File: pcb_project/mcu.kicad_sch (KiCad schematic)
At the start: 29 parts, among them J3 Conn_ST_STDC14, SW2 SW_SPDT, SW3 SW_SPST, U2 STM32U595VJTx, Y1 48MHz

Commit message: Fix more footprints and add MicroSD reader 3D model
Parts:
- C76, C77: footprint (none) -> Capacitor_SMD:C_0603_1608Metric_Pad1.08x0.95mm_HandSolder
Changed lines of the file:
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@@
 			)
 		)
-		(property "Footprint" ""
+		(property "Footprint" "Capacitor_SMD:C_0603_1608Metric_Pad1.08x0.95mm_HandSolder"
 			(at 181.61 20.6248 0)
 			(effects
@@
 			)
 		)
-		(property "Footprint" ""
+		(property "Footprint" "Capacitor_SMD:C_0603_1608Metric_Pad1.08x0.95mm_HandSolder"
 			(at 221.9452 128.27 0)
 			(effects

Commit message: Add footprints for switches
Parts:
- SW2: footprint (none) -> Button_Switch_THT:SW_Slide_SPDT_Straight_CK_OS102011MS2Q
- SW3: footprint (none) -> Button_Switch_THT:SW_TH_Tactile_Omron_B3F-100x
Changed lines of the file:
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@@
 			)
 		)
-		(property "Footprint" ""
+		(property "Footprint" "Button_Switch_THT:SW_Slide_SPDT_Straight_CK_OS102011MS2Q"
 			(at 36.83 64.77 0)
 			(effects
@@
 			)
 		)
-		(property "Footprint" ""
+		(property "Footprint" "Button_Switch_THT:SW_TH_Tactile_Omron_B3F-100x"
 			(at 177.8 41.91 0)
 			(effects

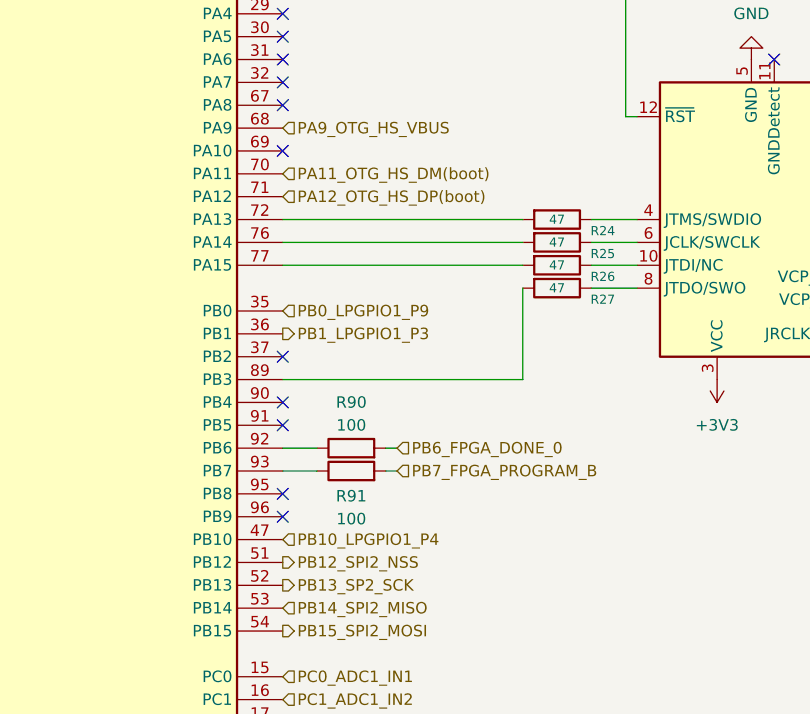
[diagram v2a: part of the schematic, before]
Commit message: Minor schematic changes for easier Layout
- Proper TVS symbol for MicroSD
- Rename USB data lines net name to allow for differential routing
- Change SDMMC_CD GPIO to easier MCU pin
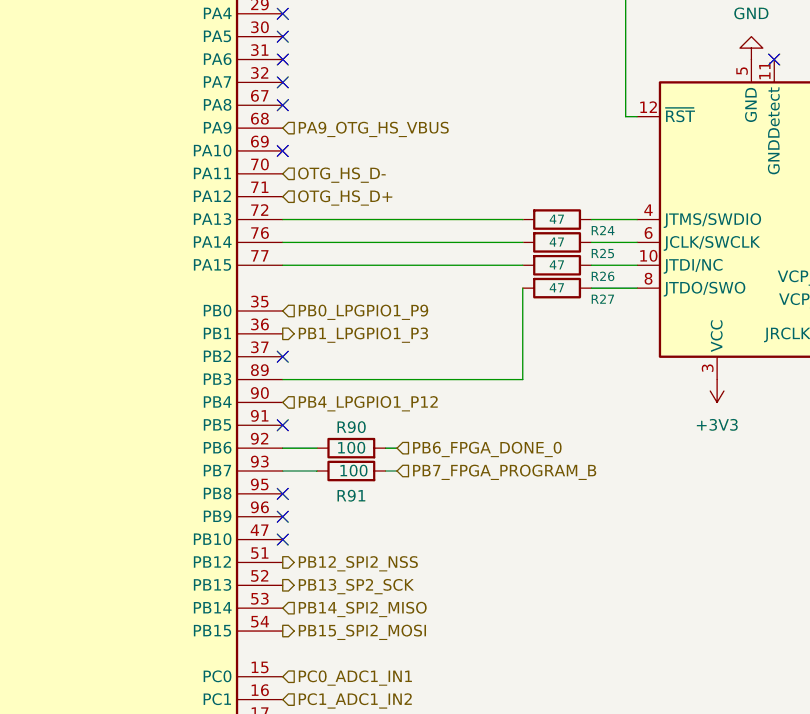
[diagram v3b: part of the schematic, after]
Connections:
- net PB4_LPGPIO1_P12: now reaches U2.90 (PB4)
- net PA11_OTG_HS_DM(boot) renamed OTG_HS_D-
- net PA12_OTG_HS_DP(boot) renamed OTG_HS_D+
- net PB10_LPGPIO1_P4: no longer names the net of U2.47 (PB10)
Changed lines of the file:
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@@
-	)
-	(no_connect
-		(at 124.46 92.71)
 	)
 	(no_connect
@@
 	(no_connect
 		(at 78.74 80.01)
+	)
+	(no_connect
+		(at 124.46 107.95)
 	)
 	(no_connect
@@
 		)
 	)
-	(hierarchical_label "PA12_OTG_HS_DP(boot)"
+	(hierarchical_label "OTG_HS_D+"
 		(shape input)
 		(at 124.46 69.85 0)
@@
 		)
 	)
-	(hierarchical_label "PA11_OTG_HS_DM(boot)"
+	(hierarchical_label "OTG_HS_D-"
 		(shape input)
 		(at 124.46 67.31 0)
@@
 		)
 	)
+	(hierarchical_label "PB4_LPGPIO1_P12"
+		(shape input)
+		(at 124.46 92.71 0)
+		(effects
+			(font
+				(size 1.27 1.27)
+			)
+			(justify left)
+		)
+	)
 	(hierarchical_label "PA9_OTG_HS_VBUS"
 		(shape input)
@@
 			)
 			(justify right)
-		)
-	)
-	(hierarchical_label "PB10_LPGPIO1_P4"
-		(shape input)
-		(at 124.46 107.95 0)
-		(effects
-			(font
-				(size 1.27 1.27)
-			)
-			(justify left)
 		)
 	)
@@
 		(dnp no)
 		(property "Reference" "R90"
-			(at 132.08 92.71 90)
+			(at 132.08 95.504 90)
 			(effects
 				(font
@@
 		)
 		(property "Value" "100"
-			(at 132.08 95.25 90)
+			(at 132.08 97.79 90)
 			(effects
 				(font
@@
 		)
 		(property "Value" "100"
-			(at 132.08 105.664 90)
-			(effects
-				(font
+			(at 132.334 100.33 90)
+			(effects
+				(font

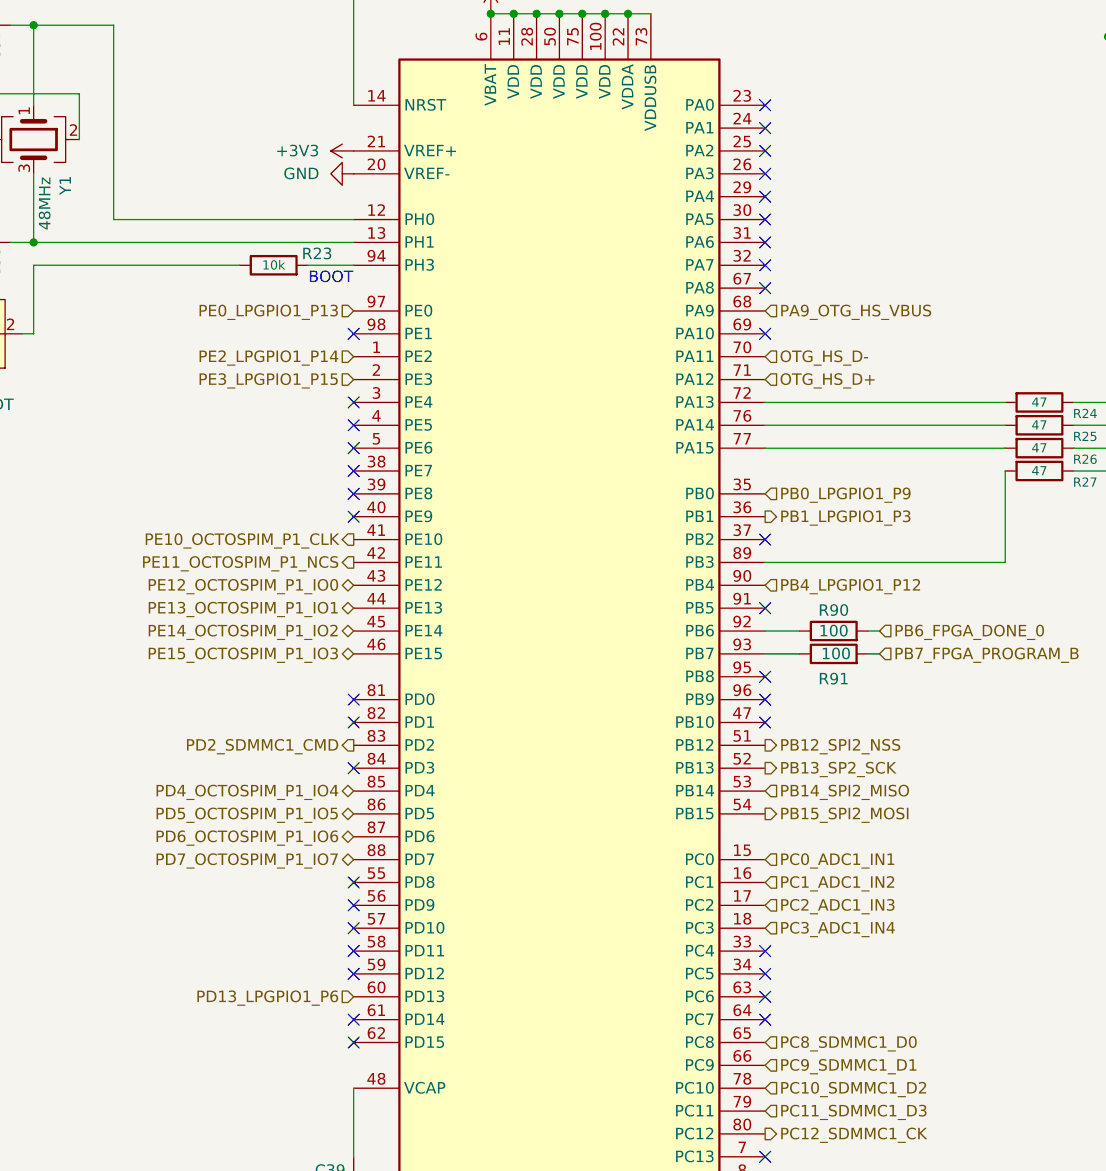
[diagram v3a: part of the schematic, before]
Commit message: Custom controller layout and some pin changes
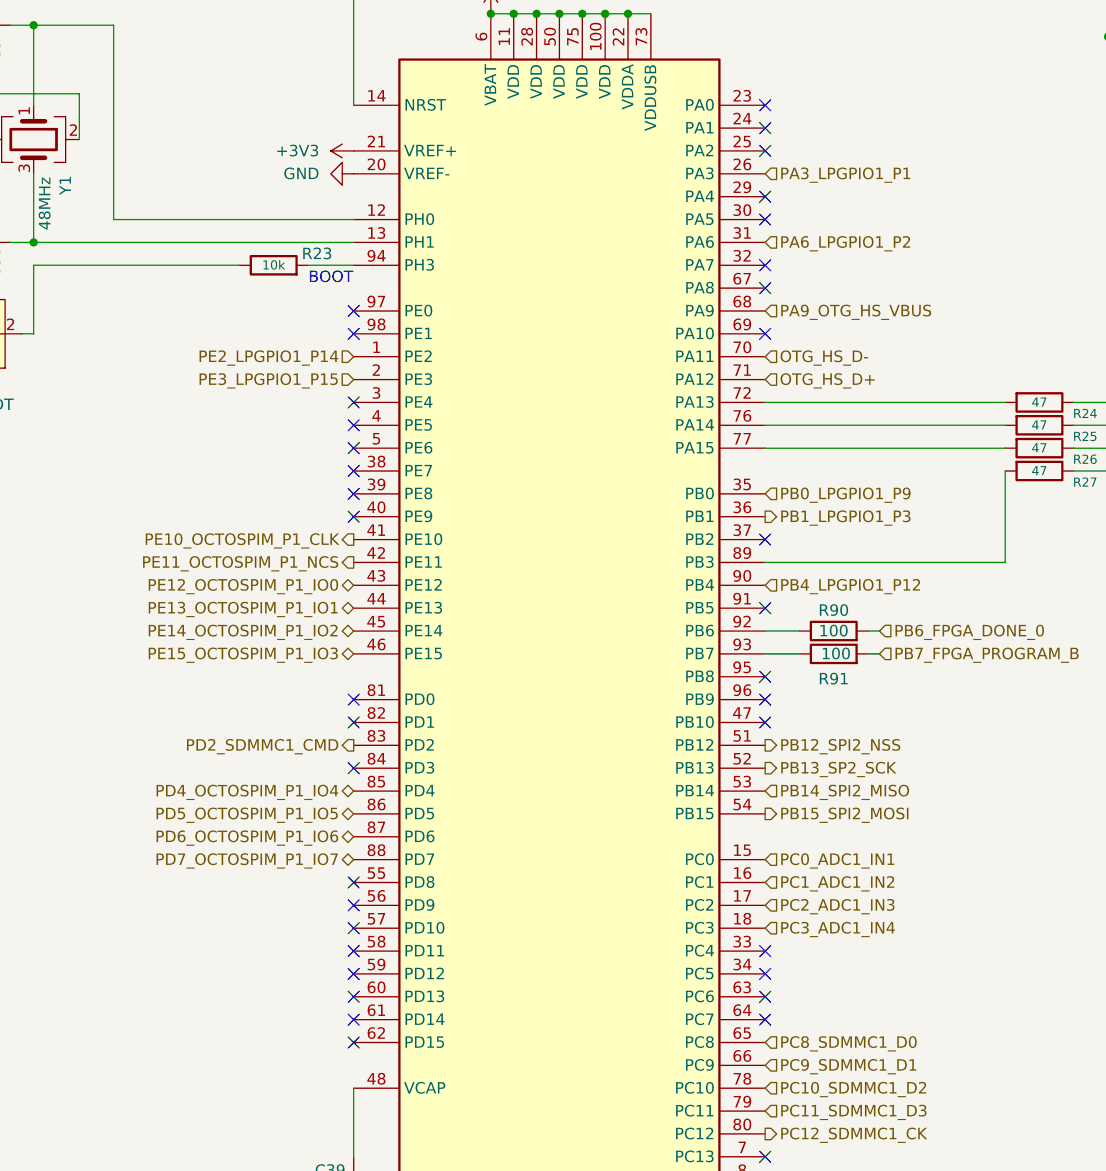
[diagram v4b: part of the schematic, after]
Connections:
- net PA3_LPGPIO1_P1: now reaches U2.26 (PA3)
- net PA6_LPGPIO1_P2: now reaches U2.31 (PA6)
- net PD13_LPGPIO1_P6: no longer names the net of U2.60 (PD13)
- net PE0_LPGPIO1_P13: no longer names the net of U2.97 (PE0)
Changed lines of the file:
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@@
-	)
-	(no_connect
-		(at 124.46 46.99)
 	)
 	(no_connect
@@
 	)
 	(no_connect
+		(at 78.74 138.43)
+	)
+	(no_connect
 		(at 78.74 107.95)
 	)
 	(no_connect
-		(at 124.46 54.61)
-	)
-	(no_connect
 		(at 78.74 77.47)
 	)
@@
 	(no_connect
 		(at 124.46 87.63)
+	)
+	(no_connect
+		(at 78.74 62.23)
 	)
 	(no_connect
@@
 		)
 	)
-	(hierarchical_label "PD13_LPGPIO1_P6"
-		(shape input)
-		(at 78.74 138.43 180)
-		(effects
-			(font
-				(size 1.27 1.27)
-			)
-			(justify right)
-		)
-	)
 	(hierarchical_label "PD5_OCTOSPIM_P1_IO5"
 		(shape bidirectional)
@@
 		)
 	)
+	(hierarchical_label "PA6_LPGPIO1_P2"
+		(shape input)
+		(at 124.46 54.61 0)
+		(effects
+			(font
+				(size 1.27 1.27)
+			)
+			(justify left)
+		)
+	)
 	(hierarchical_label "PE15_OCTOSPIM_P1_IO3"
 		(shape bidirectional)
@@
 		)
 	)
+	(hierarchical_label "PA3_LPGPIO1_P1"
+		(shape input)
+		(at 124.46 46.99 0)
+		(effects
+			(font
+				(size 1.27 1.27)
+			)
+			(justify left)
+		)
+	)
 	(hierarchical_label "PB6_FPGA_DONE_0"
 		(shape input)
@@
 		(effects
 			(font
-				(size 1.27 1.27)
-			)
-			(justify right)
-		)
-	)
-	(hierarchical_label "PE0_LPGPIO1_P13"
-		(shape input)
-		(at 78.74 62.23 180)
-		(effects
-			(font

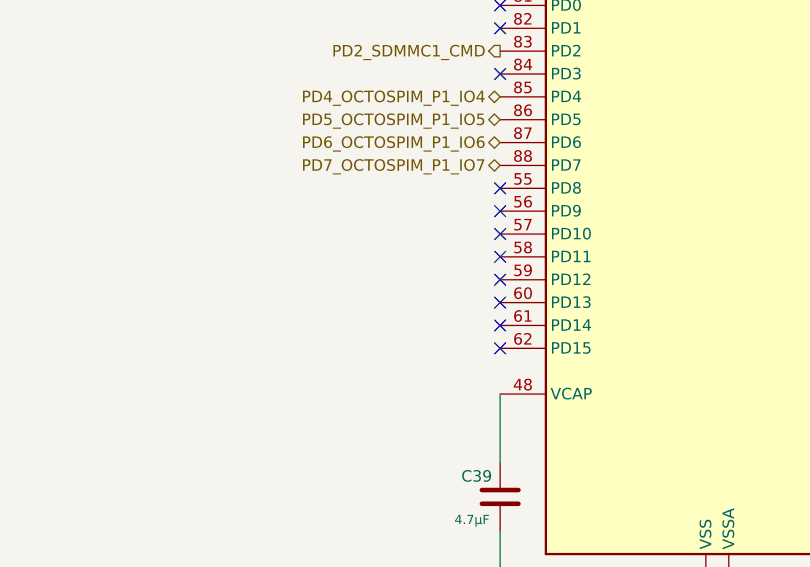
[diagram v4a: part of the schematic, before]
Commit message: Add GPIO pins for MCU and FPGA
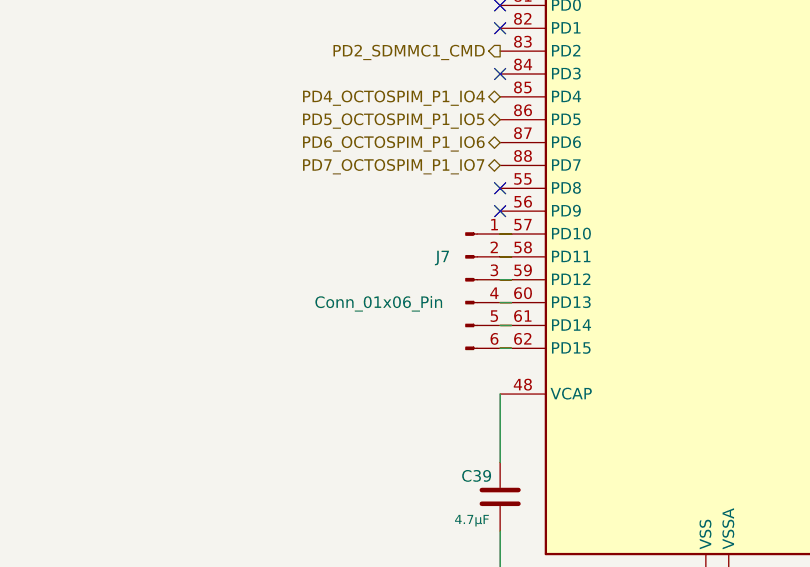
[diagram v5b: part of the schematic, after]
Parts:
- added J7: Conn_01x06_Pin, Connector_PinHeader_2.54mm:PinHeader_1x06_P2.54mm_Vertical, symbol Connector:Conn_01x06_Pin
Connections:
- net at U2.57 (PD10): now also J7.1 (Pin_1)
- net at U2.58 (PD11): now also J7.2 (Pin_2)
- net at U2.59 (PD12): now also J7.3 (Pin_3)
- net at U2.60 (PD13): now also J7.4 (Pin_4)
- net at U2.61 (PD14): now also J7.5 (Pin_5)
- net at U2.62 (PD15): now also J7.6 (Pin_6)
- no-connect marks 43 -> 37
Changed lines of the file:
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@@
-	)
-	(no_connect
-		(at 78.74 143.51)
 	)
 	(no_connect
@@
 	)
 	(no_connect
-		(at 78.74 135.89)
-	)
-	(no_connect
 		(at 189.23 78.74)
 	)
@@
 	)
 	(no_connect
-		(at 78.74 133.35)
-	)
-	(no_connect
 		(at 124.46 158.75)
 	)
@@
 	)
 	(no_connect
-		(at 78.74 130.81)
-	)
-	(no_connect
 		(at 124.46 95.25)
 	)
@@
 	)
 	(no_connect
-		(at 78.74 140.97)
-	)
-	(no_connect
 		(at 78.74 72.39)
 	)
@@
 	)
 	(no_connect
-		(at 78.74 138.43)
-	)
-	(no_connect
 		(at 78.74 107.95)
 	)
@@
 	(wire
 		(pts
+			(xy 80.01 135.89) (xy 78.74 135.89)
+		)
+		(stroke
+			(width 0)
+			(type default)
+		)
+	)
+	(wire
+		(pts
 			(xy 220.98 53.34) (xy 232.41 53.34)
 		)
@@
 	(wire
 		(pts
+			(xy 80.01 133.35) (xy 78.74 133.35)
+		)
+		(stroke
+			(width 0)
+			(type default)
+		)
+	)
+	(wire
+		(pts
 			(xy 163.83 80.01) (xy 158.75 80.01)
 		)
@@
 	(wire
 		(pts
+			(xy 80.01 138.43) (xy 78.74 138.43)
+		)
+		(stroke
+			(width 0)
+			(type default)
+		)
+	)
+	(wire
+		(pts
+			(xy 80.01 140.97) (xy 78.74 140.97)
+		)
+		(stroke
+			(width 0)
+			(type default)
+		)
+	)
+	(wire
+		(pts
 			(xy 247.65 29.21) (xy 255.27 29.21)
 		)
@@
 	(wire
 		(pts
+			(xy 80.01 143.51) (xy 78.74 143.51)
+		)
+		(stroke
+			(width 0)
+			(type default)
+		)
+	)
+	(wire
+		(pts
 			(xy 220.98 76.2) (xy 232.41 76.2)
 		)
@@
 		(pts
 			(xy 170.18 31.75) (xy 173.99 31.75)
+		)
+		(stroke
+			(width 0)
+			(type default)
+		)
+	)
+	(wire
+		(pts
+			(xy 80.01 130.81) (xy 78.74 130.81)
 		)
 		(stroke
@@
 					(unit 1)
 				)
+			)
+		)
+	)
+	(symbol
+		(lib_id "Connector:Conn_01x06_Pin")
+		(at 74.93 135.89 0)
+		(unit 1)
+		(exclude_from_sim no)
+		(in_bom yes)
+		(on_board yes)
+		(dnp no)
+		(property "Reference" "J7"
+			(at 72.39 133.35 0)
+			(effects
+				(font
+					(size 1.27 1.27)
+				)
+			)
+		)
+		(property "Value" "Conn_01x06_Pin"
+			(at 65.278 138.43 0)
+			(effects
+				(font
+					(size 1.27 1.27)
+				)
+			)
+		)
+		(property "Footprint" "Connector_PinHeader_2.54mm:PinHeader_1x06_P2.54mm_Vertical"
+			(at 74.93 135.89 0)
+			(effects
+				(font
+					(size 1.27 1.27)
+				)
+				(hide yes)
+			)
+		)
+		(property "Datasheet" "~"
+			(at 74.93 135.89 0)
+			(effects
+				(font
+					(size 1.27 1.27)
+				)
+				(hide yes)
+			)
+		)
+		(property "Description" "Generic connector, single row, 01x06, script generated"
+			(at 74.93 135.89 0)
+			(effects
+				(font
+					(size 1.27 1.27)
+				)
+				(hide yes)
+			)
+		)
+		(pin "1"
+		)
+		(pin "2"
+		)
+		(pin "3"
+		)
+		(pin "4"
+		)
+		(pin "5"
+		)
+		(pin "6"
+		)
+		(instances
+			(project ""
+				(path "/98f80f66-4595-4d0f-90ca-59b2db6f447b/1a3eaa4f-d49c-486a-8882-cdef72ae86f4"
+					(reference "J7")
+					(unit 1)
+				)
